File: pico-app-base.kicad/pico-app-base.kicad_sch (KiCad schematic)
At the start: 26 parts, among them J1 Conn_EYESPI, J2 Conn_Dummy, J5 Stemma-QT_Qwicc, Q1 AO3401A, Q2 AO3401A, SW1 SW_ON, SW3 SW_RST, U1 PCF8563T, U2 74LVC2G74, U5 XTSD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

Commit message: added zones and connections
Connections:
- net +BAT renamed +BATT
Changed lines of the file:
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@@
   (title_block
     (title "pico-app-base")
-    (date "2024-05-16")
-    (rev "0.86")
+    (date "2024-05-28")
+    (rev "0.87")
     (company "Bernhard Bablok")
     (comment 1 "https://github.com/bablokb/pcb-pico-app-base")
@@
     (stroke (width 0) (type default))
   )
-  (wire (pts (xy 257.81 83.82) (xy 265.43 83.82))
-    (stroke (width 0) (type default))
-  )
   (wire (pts (xy 107.95 43.18) (xy 107.95 55.88))
     (stroke (width 0) (type default))
@@
     (stroke (width 0) (type default))
   )
-  (wire (pts (xy 262.89 110.49) (xy 267.97 110.49))
+  (wire (pts (xy 262.89 110.49) (xy 270.51 110.49))
     (stroke (width 0) (type default))
   )
@@
     )
   )
-  (global_label "+BAT" (shape input) (at 257.81 83.82 180) (fields_autoplaced)
-    (effects (font (size 1.27 1.27)) (justify right))
-    (property "Intersheetrefs" "${INTERSHEET_REFS}" (at 250.5804 83.82 0)
-      (effects (font (size 1.27 1.27)) (justify right) hide)
-    )
-  )
   (global_label "GP10" (shape bidirectional) (at 30.48 39.37 180) (fields_autoplaced)
     (effects (font (size 1.27 1.27)) (justify right))
@@
     )
   )
-  (global_label "+BAT" (shape input) (at 238.76 22.86 180) (fields_autoplaced)
-    (effects (font (size 1.27 1.27)) (justify right))
-    (property "Intersheetrefs" "${INTERSHEET_REFS}" (at 231.5304 22.86 0)
-      (effects (font (size 1.27 1.27)) (justify right) hide)
-    )
-  )
   (global_label "GP4_DONE" (shape bidirectional) (at 267.97 35.56 0) (fields_autoplaced)
     (effects (font (size 1.27 1.27)) (justify left))
@@
     )
   )
-  (global_label "+BAT" (shape input) (at 267.97 110.49 0) (fields_autoplaced)
-    (effects (font (size 1.27 1.27)) (justify left))
-    (property "Intersheetrefs" "${INTERSHEET_REFS}" (at 275.1996 110.49 0)
-      (effects (font (size 1.27 1.27)) (justify left) hide)
-    )
-  )
   (global_label "SDA" (shape bidirectional) (at 152.4 91.44 180) (fields_autoplaced)
     (effects (font (size 1.27 1.27)) (justify right))
@@
     (property "Intersheetrefs" "${INTERSHEET_REFS}" (at 64.77 45.72 0)
       (effects (font (size 1.27 1.27)) hide)
-    )
-  )
-  (global_label "+BAT" (shape input) (at 160.02 26.67 180) (fields_autoplaced)
-    (effects (font (size 1.27 1.27)) (justify right))
-    (property "Intersheetrefs" "${INTERSHEET_REFS}" (at 152.7904 26.67 0)
-      (effects (font (size 1.27 1.27)) (justify right) hide)
     )
   )
@@
     )
   )
+  (symbol (lib_id "power:+BATT") (at 238.76 22.86 0) (mirror y) (unit 1)
+    (in_bom yes) (on_board yes) (dnp no)
+    (property "Reference" "#PWR016" (at 238.76 26.67 0)
+      (effects (font (size 1.27 1.27)) hide)
+    )
+    (property "Value" "+BATT" (at 234.95 21.59 0)
+      (effects (font (size 1.27 1.27)))
+    )
+    (property "Footprint" "" (at 238.76 22.86 0)
+      (effects (font (size 1.27 1.27)) hide)
+    )
+    (property "Datasheet" "" (at 238.76 22.86 0)
+      (effects (font (size 1.27 1.27)) hide)
+    )
+    (pin "1")
+    (instances
+      (project "pico-app-base"
+        (path "/17133424-0baa-43c4-a5ff-fd6573e84d8e"
+          (reference "#PWR016") (unit 1)
+        )
+      )
+    )
+  )
   (symbol (lib_id "power:GND") (at 144.78 36.83 270) (unit 1)
     (in_bom yes) (on_board yes) (dnp no)
@@
     )
   )
+  (symbol (lib_id "power:+BATT") (at 270.51 110.49 270) (mirror x) (unit 1)
+    (in_bom yes) (on_board yes) (dnp no)
+    (property "Reference" "#PWR020" (at 266.7 110.49 0)
+      (effects (font (size 1.27 1.27)) hide)
+    )
+    (property "Value" "+BATT" (at 273.05 107.95 90)
+      (effects (font (size 1.27 1.27)))
+    )
+    (property "Footprint" "" (at 270.51 110.49 0)
+      (effects (font (size 1.27 1.27)) hide)
+    )
+    (property "Datasheet" "" (at 270.51 110.49 0)
+      (effects (font (size 1.27 1.27)) hide)
+    )
+    (pin "1")
+    (instances
+      (project "pico-app-base"
+        (path "/17133424-0baa-43c4-a5ff-fd6573e84d8e"
+          (reference "#PWR020") (unit 1)
+        )
+      )
+    )
+  )
   (symbol (lib_id "power:PWR_FLAG") (at 265.43 95.25 270) (unit 1)
     (in_bom yes) (on_board yes) (dnp no) (fields_autoplaced)
@@
     )
   )
-  (symbol (lib_id "power:PWR_FLAG") (at 265.43 83.82 270) (unit 1)
-    (in_bom yes) (on_board yes) (dnp no) (fields_autoplaced)
-    (property "Reference" "#FLG0101" (at 267.335 83.82 0)
-      (effects (font (size 1.27 1.27)) hide)
-    )
-    (property "Value" "PWR_FLAG" (at 268.605 84.2538 90)
-      (effects (font (size 1.27 1.27)) (justify left))
-    )
-    (property "Footprint" "" (at 265.43 83.82 0)
-      (effects (font (size 1.27 1.27)) hide)
-    )
-    (property "Datasheet" "~" (at 265.43 83.82 0)
-      (effects (font (size 1.27 1.27)) hide)
-    )
-    (pin "1")
-    (instances
-      (project "pico-app-base"
-        (path "/17133424-0baa-43c4-a5ff-fd6573e84d8e"
-          (reference "#FLG0101") (unit 1)
-        )
-      )
-    )
-  )
   (symbol (lib_id "power:PWR_FLAG") (at 219.71 83.82 90) (unit 1)
     (in_bom yes) (on_board yes) (dnp no) (fields_autoplaced)
@@
         )
       )
+    )
+  )
+  (symbol (lib_id "power:+BATT") (at 160.02 26.67 0) (mirror y) (unit 1)
+    (in_bom yes) (on_board yes) (dnp no)
+    (property "Reference" "#PWR017" (at 160.02 30.48 0)
+      (effects (font (size 1.27 1.27)) hide)
+    )
+    (property "Value" "+BATT" (at 154.94 25.4 0)
+      (effects (font (size 1.27 1.27)))
+    )
+    (property "Footprint" "" (at 160.02 26.67 0)
+      (effects (font (size 1.27 1.27)) hide)
+    )
+    (property "Datasheet" "" (at 160.02 26.67 0)
+      (effects (font (size 1.27 1.27)) hide)
+    )
+    (pin "1")
+    (instances
+      (project "pico-app-base"
+        (path "/17133424-0baa-43c4-a5ff-fd6573e84d8e"
+          (reference "#PWR017") (unit 1)
+        )
+      )

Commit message: switched order of mosfets
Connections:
- net +BATT: now also Q1.3 (D); no longer C1.1, C2.1, Q2.2 (S), R2.1, U1.8 (VDD), U2.7 (~{PRE}), U2.8 (VCC)
- net VSYS: now also Q2.3 (D); no longer Q1.2 (S)
- new net VCC: C1.1, C2.1, Q1.2 (S), Q2.2 (S), R2.1, U1.8 (VDD), U2.7 (~{PRE}), U2.8 (VCC)
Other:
- moved on the sheet: Q1, Q2

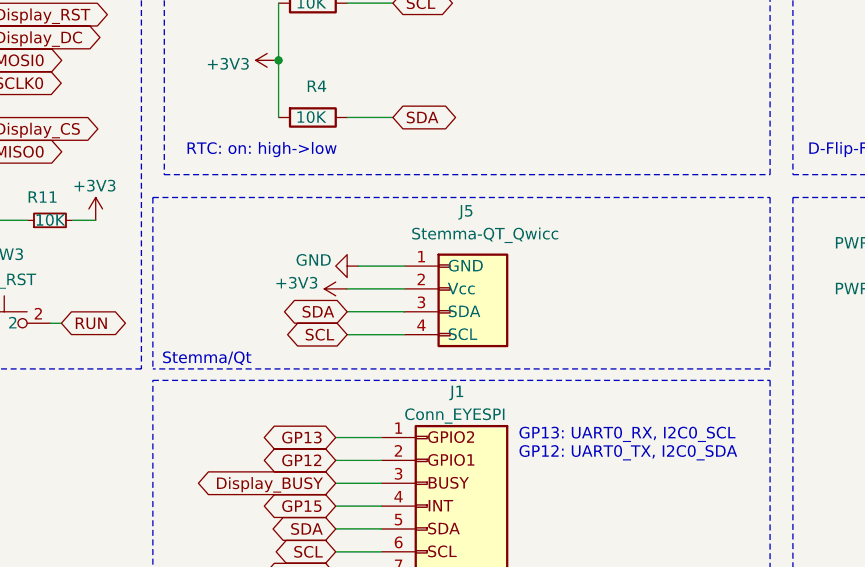
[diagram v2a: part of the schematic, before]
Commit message: added I2C-grove, completed routing
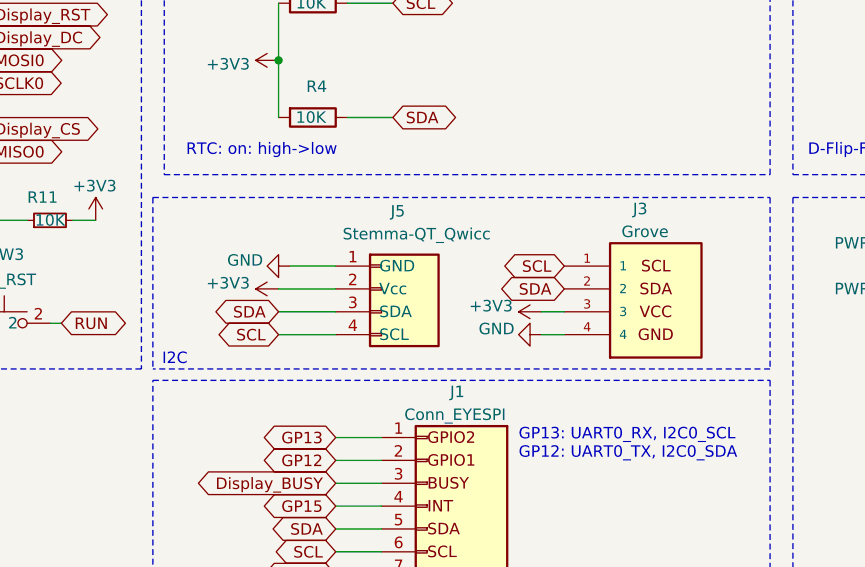
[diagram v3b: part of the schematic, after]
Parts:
- added J3: Grove, user:grove_vertical, symbol user:Grove
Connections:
- net +3V3: now also J3.3
- net GND: now also J3.4
- net SCL: now also J3.1
- net SDA: now also J3.2
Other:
- note added: "I2C"
- note removed: "Stemma/Qt"
- moved on the sheet: J5
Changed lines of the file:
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@@
   (title_block
     (title "pico-app-base")
-    (date "2024-06-10")
-    (rev "0.90")
+    (date "2024-06-20")
+    (rev "0.91")
     (company "Bernhard Bablok")
     (comment 1 "https://github.com/bablokb/pcb-pico-app-base")
@@
     (stroke (width 0) (type dash))
   )
+  (wire (pts (xy 173.99 91.44) (xy 176.53 91.44))
+    (stroke (width 0) (type default))
+  )
   (polyline (pts (xy 132.08 76.2) (xy 199.39 76.2))
     (stroke (width 0) (type dash))
@@
     (stroke (width 0) (type default))
   )
-  (wire (pts (xy 152.4 91.44) (xy 158.75 91.44))
+  (wire (pts (xy 144.78 91.44) (xy 151.13 91.44))
     (stroke (width 0) (type default))
   )
@@
     (stroke (width 0) (type default))
   )
+  (wire (pts (xy 173.99 93.98) (xy 176.53 93.98))
+    (stroke (width 0) (type default))
+  )
   (wire (pts (xy 64.77 25.4) (xy 69.85 25.4))
     (stroke (width 0) (type default))
@@
     (stroke (width 0) (type default))
   )
-  (wire (pts (xy 152.4 93.98) (xy 158.75 93.98))
+  (wire (pts (xy 144.78 93.98) (xy 151.13 93.98))
     (stroke (width 0) (type default))
   )
@@
     (stroke (width 0) (type default))
   )
-  (wire (pts (xy 153.67 86.36) (xy 158.75 86.36))
-    (stroke (width 0) (type default))
-  )
-  (wire (pts (xy 152.4 88.9) (xy 158.75 88.9))
+  (wire (pts (xy 146.05 86.36) (xy 151.13 86.36))
+    (stroke (width 0) (type default))
+  )
+  (wire (pts (xy 144.78 88.9) (xy 151.13 88.9))
     (stroke (width 0) (type default))
   )
@@
     (effects (font (size 1.27 1.27)) (justify left bottom))
   )
-  (text "Stemma/Qt" (at 131.826 97.536 0)
+  (text "I2C" (at 131.826 97.536 0)
     (effects (font (size 1.27 1.27)) (justify left bottom))
   )
@@
     )
   )
-  (global_label "SCL" (shape bidirectional) (at 152.4 93.98 180) (fields_autoplaced)
-    (effects (font (size 1.27 1.27)) (justify right))
-    (property "Intersheetrefs" "${INTERSHEET_REFS}" (at 152.4 93.98 0)
+  (global_label "SCL" (shape bidirectional) (at 144.78 93.98 180) (fields_autoplaced)
+    (effects (font (size 1.27 1.27)) (justify right))
+    (property "Intersheetrefs" "${INTERSHEET_REFS}" (at 144.78 93.98 0)
       (effects (font (size 1.27 1.27)) hide)
     )
@@
     )
   )
+  (global_label "SDA" (shape bidirectional) (at 176.53 88.9 180) (fields_autoplaced)
+    (effects (font (size 1.27 1.27)) (justify right))
+    (property "Intersheetrefs" "${INTERSHEET_REFS}" (at 176.53 88.9 0)
+      (effects (font (size 1.27 1.27)) hide)
+    )
+  )
   (global_label "~{INT}" (shape bidirectional) (at 220.98 43.18 180) (fields_autoplaced)
     (effects (font (size 1.27 1.27)) (justify right))
@@
     )
   )
-  (global_label "SDA" (shape bidirectional) (at 152.4 91.44 180) (fields_autoplaced)
-    (effects (font (size 1.27 1.27)) (justify right))
-    (property "Intersheetrefs" "${INTERSHEET_REFS}" (at 152.4 91.44 0)
+  (global_label "SDA" (shape bidirectional) (at 144.78 91.44 180) (fields_autoplaced)
+    (effects (font (size 1.27 1.27)) (justify right))
+    (property "Intersheetrefs" "${INTERSHEET_REFS}" (at 144.78 91.44 0)
       (effects (font (size 1.27 1.27)) hide)
     )
@@
     (effects (font (size 1.27 1.27)) (justify left))
     (property "Intersheetrefs" "${INTERSHEET_REFS}" (at 111.76 48.26 0)
+      (effects (font (size 1.27 1.27)) hide)
+    )
+  )
+  (global_label "SCL" (shape bidirectional) (at 176.53 86.36 180) (fields_autoplaced)
+    (effects (font (size 1.27 1.27)) (justify right))
+    (property "Intersheetrefs" "${INTERSHEET_REFS}" (at 176.53 86.36 0)
       (effects (font (size 1.27 1.27)) hide)
     )
@@
     )
   )
+  (symbol (lib_id "power:+3V3") (at 173.99 91.44 90) (unit 1)
+    (in_bom yes) (on_board yes) (dnp no)
+    (property "Reference" "#PWR038" (at 177.8 91.44 0)
+      (effects (font (size 1.27 1.27)) hide)
+    )
+    (property "Value" "+3V3" (at 170.815 90.805 90)
+      (effects (font (size 1.27 1.27)) (justify left))
+    )
+    (property "Footprint" "" (at 173.99 91.44 0)
+      (effects (font (size 1.27 1.27)) hide)
+    )
+    (property "Datasheet" "" (at 173.99 91.44 0)
+      (effects (font (size 1.27 1.27)) hide)
+    )
+    (pin "1")
+    (instances
+      (project "pico-app-base"
+        (path "/17133424-0baa-43c4-a5ff-fd6573e84d8e"
+          (reference "#PWR038") (unit 1)
+        )
+      )
+    )
+  )
   (symbol (lib_id "power:+3V3") (at 229.87 151.13 90) (unit 1)
     (in_bom yes) (on_board yes) (dnp no)
@@
     )
   )
-  (symbol (lib_id "user:Stemma-QT_Qwicc") (at 163.83 88.9 0) (unit 1)
+  (symbol (lib_id "user:Stemma-QT_Qwicc") (at 156.21 88.9 0) (unit 1)
     (in_bom no) (on_board yes) (dnp no)
-    (property "Reference" "J5" (at 164.846 80.264 0)
-      (effects (font (size 1.27 1.27)) (justify left))
-    )
-    (property "Value" "Stemma-QT_Qwicc" (at 159.512 82.804 0)
-      (effects (font (size 1.27 1.27)) (justify left))
-    )
-    (property "Footprint" "Connector_JST:JST_SH_SM04B-SRSS-TB_1x04-1MP_P1.00mm_Horizontal" (at 163.83 88.9 0)
-      (effects (font (size 1.27 1.27)) hide)
-    )
-    (property "Datasheet" "~" (at 163.83 88.9 0)
-      (effects (font (size 1.27 1.27)) hide)
-    )
-    (property "LCSC" "C160404" (at 163.83 88.9 0)
+    (property "Reference" "J5" (at 157.226 80.264 0)
+      (effects (font (size 1.27 1.27)) (justify left))
+    )
+    (property "Value" "Stemma-QT_Qwicc" (at 151.892 82.804 0)
+      (effects (font (size 1.27 1.27)) (justify left))
+    )
+    (property "Footprint" "Connector_JST:JST_SH_SM04B-SRSS-TB_1x04-1MP_P1.00mm_Horizontal" (at 156.21 88.9 0)
+      (effects (font (size 1.27 1.27)) hide)
+    )
+    (property "Datasheet" "~" (at 156.21 88.9 0)
+      (effects (font (size 1.27 1.27)) hide)
+    )
+    (property "LCSC" "C160404" (at 156.21 88.9 0)
       (effects (font (size 1.27 1.27)) hide)
     )
@@
     )
   )
-  (symbol (lib_id "power:+3V3") (at 152.4 88.9 90) (unit 1)
-    (in_bom yes) (on_board yes) (dnp no)
-    (property "Reference" "#PWR015" (at 156.21 88.9 0)
-      (effects (font (size 1.27 1.27)) hide)
-    )
-    (property "Value" "+3V3" (at 149.225 88.265 90)
-      (effects (font (size 1.27 1.27)) (justify left))
-    )
-    (property "Footprint" "" (at 152.4 88.9 0)
-      (effects (font (size 1.27 1.27)) hide)
-    )
-    (property "Datasheet" "" (at 152.4 88.9 0)
+  (symbol (lib_id "power:+3V3") (at 144.78 88.9 90) (unit 1)
+    (in_bom yes) (on_board yes) (dnp no)
+    (property "Reference" "#PWR015" (at 148.59 88.9 0)
+      (effects (font (size 1.27 1.27)) hide)
+    )
+    (property "Value" "+3V3" (at 141.605 88.265 90)
+      (effects (font (size 1.27 1.27)) (justify left))
+    )
+    (property "Footprint" "" (at 144.78 88.9 0)
+      (effects (font (size 1.27 1.27)) hide)
+    )
+    (property "Datasheet" "" (at 144.78 88.9 0)
       (effects (font (size 1.27 1.27)) hide)
     )
@@
         (path "/17133424-0baa-43c4-a5ff-fd6573e84d8e"
           (reference "#PWR015") (unit 1)
+        )
+      )
+    )
+  )
+  (symbol (lib_id "power:GND") (at 173.99 93.98 270) (unit 1)
+    (in_bom yes) (on_board yes) (dnp no)
+    (property "Reference" "#PWR030" (at 167.64 93.98 0)
+      (effects (font (size 1.27 1.27)) hide)
+    )
+    (property "Value" "GND" (at 167.005 93.345 90)
+      (effects (font (size 1.27 1.27)) (justify left))
+    )
+    (property "Footprint" "" (at 173.99 93.98 0)
+      (effects (font (size 1.27 1.27)) hide)
+    )
+    (property "Datasheet" "" (at 173.99 93.98 0)
+      (effects (font (size 1.27 1.27)) hide)
+    )
+    (pin "1")
+    (instances
+      (project "pico-app-base"
+        (path "/17133424-0baa-43c4-a5ff-fd6573e84d8e"
+          (reference "#PWR030") (unit 1)
         )
       )
@@
     )
   )
+  (symbol (lib_id "user:Grove") (at 186.69 88.9 0) (unit 1)
+    (in_bom no) (on_board yes) (dnp no)
+    (property "Reference" "J3" (at 184.15 80.01 0)
+      (effects (font (size 1.27 1.27)) (justify left))
+    )
+    (property "Value" "Grove" (at 182.88 82.55 0)
+      (effects (font (size 1.27 1.27)) (justify left))
+    )
+    (property "Footprint" "user:grove_vertical" (at 180.34 80.01 0)
+      (effects (font (size 1.27 1.27)) (justify left bottom) hide)
+    )
+    (property "Datasheet" "" (at 196.85 88.9 0)
+      (effects (font (size 1.27 1.27)) (justify left bottom) hide)
+    )
+    (property "MANUFACTURER" "Seeed Technology" (at 181.61 100.33 0)
+      (effects (font (size 1.27 1.27)) (justify left bottom) hide)
+    )
+    (pin "2")
+    (pin "3")
+    (pin "4")
+    (pin "1")
+    (instances
+      (project "pico-app-base"
+        (path "/17133424-0baa-43c4-a5ff-fd6573e84d8e"
+          (reference "J3") (unit 1)
+        )
+      )
+    )
+  )
   (symbol (lib_id "power:GND") (at 87.63 83.82 0) (unit 1)
     (in_bom yes) (on_board yes) (dnp no)
@@
     )
   )
-  (symbol (lib_id "power:GND") (at 153.67 86.36 270) (unit 1)
-    (in_bom yes) (on_board yes) (dnp no)
-    (property "Reference" "#PWR01" (at 147.32 86.36 0)
-      (effects (font (size 1.27 1.27)) hide)
-    )
-    (property "Value" "GND" (at 146.685 85.725 90)
-      (effects (font (size 1.27 1.27)) (justify left))
-    )
-    (property "Footprint" "" (at 153.67 86.36 0)
-      (effects (font (size 1.27 1.27)) hide)
-    )
-    (property "Datasheet" "" (at 153.67 86.36 0)
-      (effects (font (size 1.27 1.27)) hide)
-    )
+  (symbol (lib_id "power:GND") (at 146.05 86.36 270) (unit 1)
+    (in_bom yes) (on_board yes) (dnp no)
+    (property "Reference" "#PWR01" (at 139.7 86.36 0)
+      (effects (font (size 1.27 1.27)) hide)
+    )
+    (property "Value" "GND" (at 139.065 85.725 90)
+      (effects (font (size 1.27 1.27)) (justify left))
+    )
+    (property "Footprint" "" (at 146.05 86.36 0)
+      (effects (font (size 1.27 1.27)) hide)
+    )
+    (property "Datasheet" "" (at 146.05 86.36 0)
+      (effects (font (size 1.27 1.27)) hide)
+    )

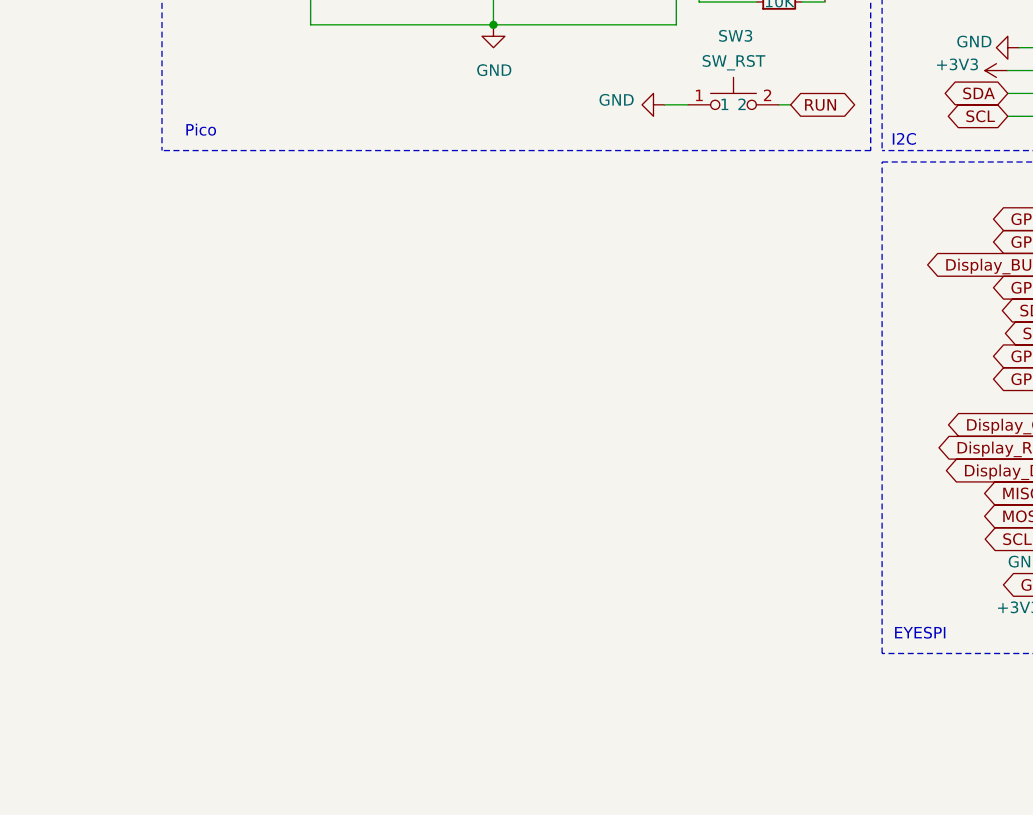
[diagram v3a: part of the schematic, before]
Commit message: added battery-fuel gauge
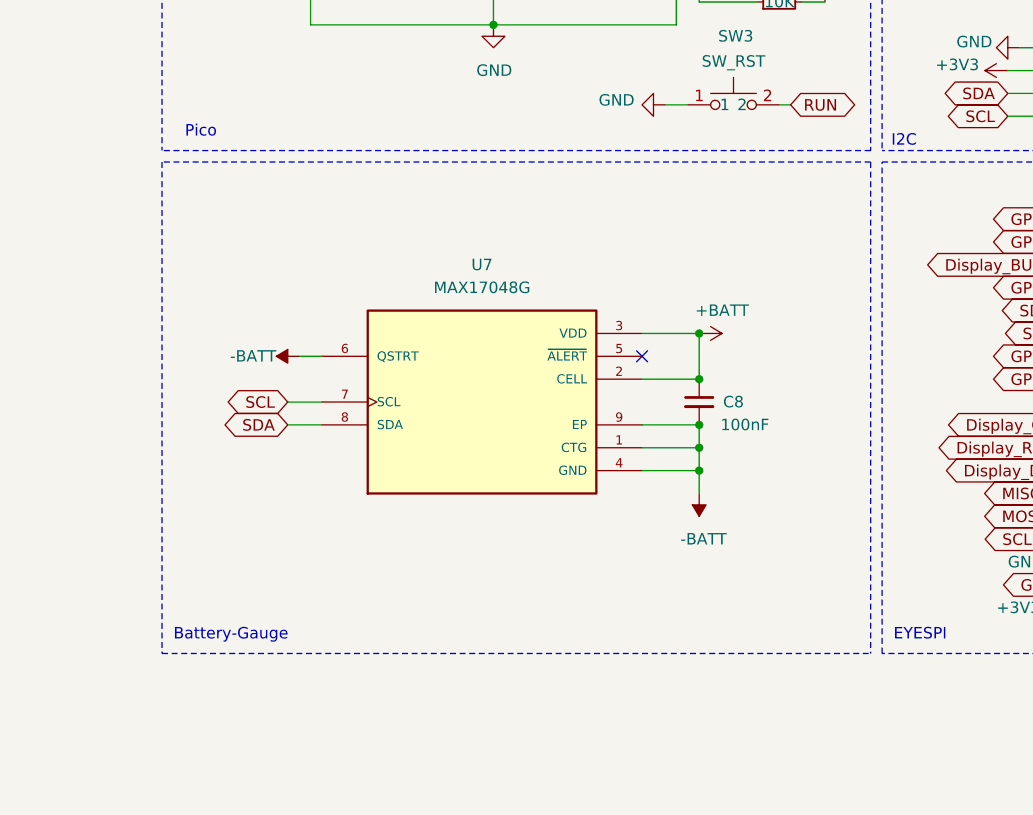
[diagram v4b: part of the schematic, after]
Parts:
- added C8: 100nF, Capacitor_SMD:C_0402_1005Metric, symbol Device:C_Small
- added U7: MAX17048G, user:MAX17048G, symbol user:MAX17048G
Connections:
- net +BATT: now also C8.1, U7.2 (CELL), U7.3 (VDD)
- net SCL: now also U7.7 (SCL)
- net SDA: now also U7.8 (SDA)
- new net -BATT: C8.2, U7.1 (CTG), U7.4 (GND), U7.6 (QSTRT), U7.9 (EP)
- no-connect marks 8 -> 9
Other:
- note added: "Battery-Gauge"
